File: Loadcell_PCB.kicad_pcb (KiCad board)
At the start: 2 copper layers, 57.5 x 74.5 mm, 52 parts, among them J1 USB_C_Receptacle_USB2.0, J2 Load cell side, J3 Micro_SD_Card, Q1 S8550, SW1 RESET, U1 ATmega328P-M, U4 HX711, U5 74125, U6 LD1117S33TR_SOT223, U7 CH340C, Y1 16MHz

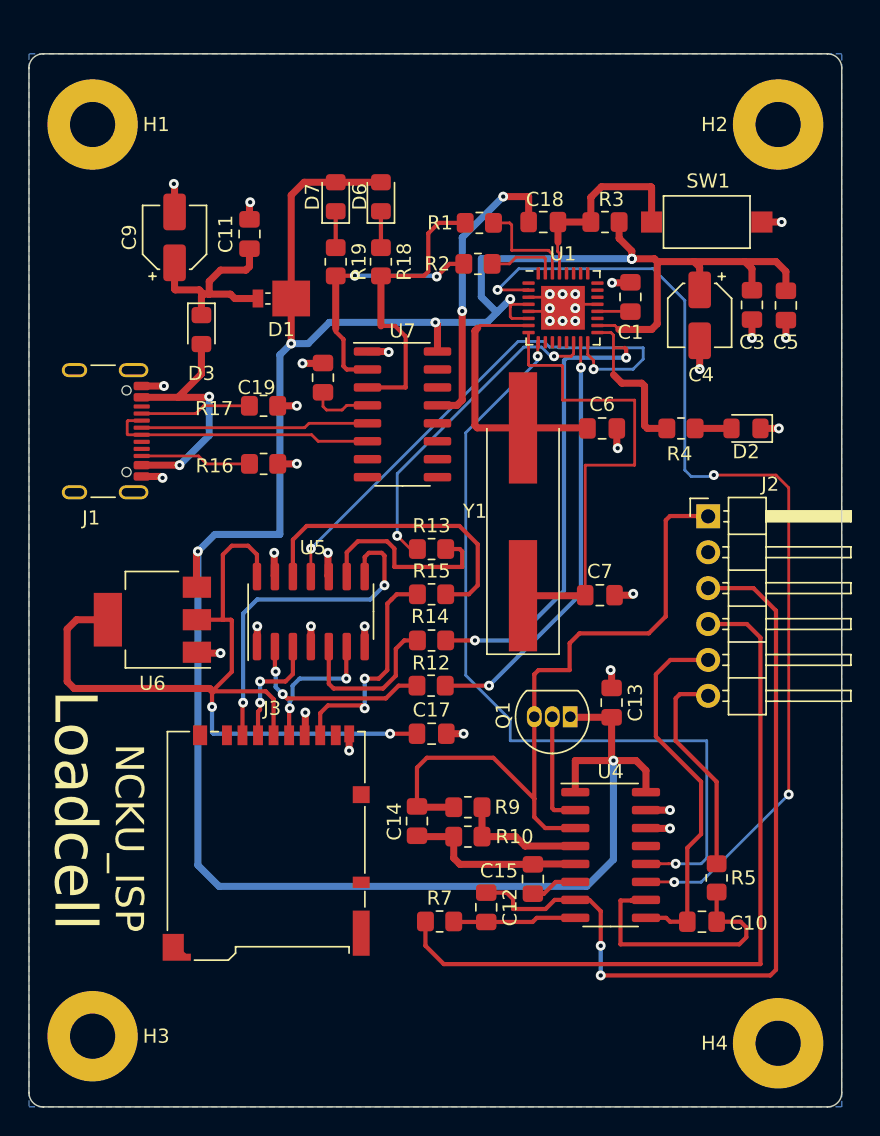
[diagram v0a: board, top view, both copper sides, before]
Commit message: some cleanup and add .gitignore
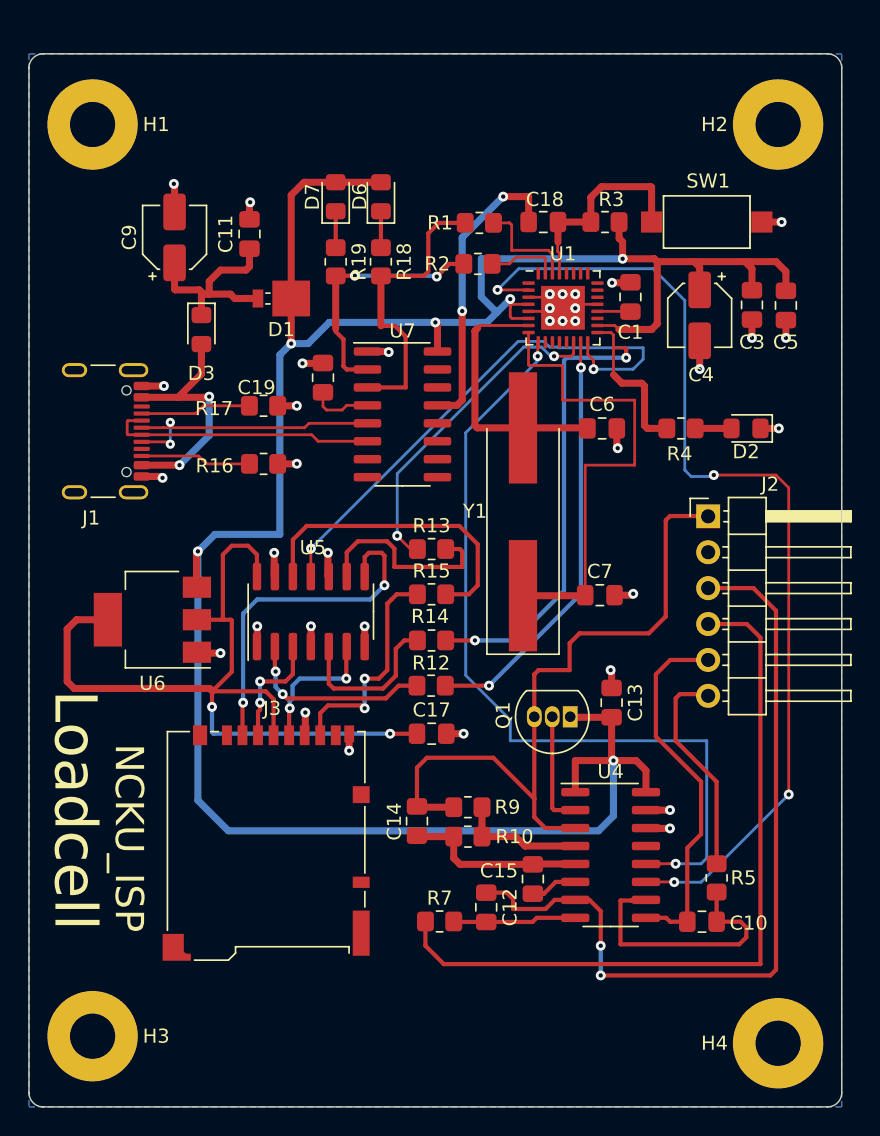
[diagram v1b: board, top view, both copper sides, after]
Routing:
- net +5V: track 181.8 -> 173.8 mm, vias 7 -> 6
- net /D+: track 16.1 -> 20.1 mm, vias 0 -> 2

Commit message: further cleanup for temp file
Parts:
- removed the C11 at (88.1, 35.1)
- removed the C4 at (120.0, 40.9)
- removed the C9 at (82.8, 35.4)
- removed the D1 at (90.4, 39.7)
- added C2: 4u7F_16V, Capacitor_SMD:CP_Elec_4x3, F.Cu at (80.9, 34.8)
- added C3: 100nF, Capacitor_SMD:C_0805_2012Metric_Pad1.18x1.45mm_HandSolder, F.Cu at (86.6, 34.7)
- C6: renamed from C5; value 1uF -> 100nF
- moved C6 2.45 mm to (123.6, 40.1)
- moved C4 2.45 mm to (126.1, 40.1)
- renumbered C12 to C11, C13 to C12, C14 to C13, C15 to C14, C17 to C15, C3 to C4, C19 to C5, C6 to C7, C7 to C8, C18 to C9, D3 to D1, D6 to D3, D7 to D4, R17 to R1, R7 to R10, R9 to R11, R10 to R12, R12 to R13, R13 to R14, R14 to R15, R15 to R16, R16 to R2, R1 to R3, R2 to R4, R3 to R5, R4 to R6, R18 to R7, R19 to R8, R5 to R9, U7 to U2, U4 to U3, U5 to U4, U6 to U5
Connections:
- D1 pad 1: VBUS -> +5V
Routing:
- net VBUS: track 15.0 -> 0.00 mm
- net +5V: track 173.8 -> 187.0 mm
- net GND: track 49.4 -> 47.6 mm, vias 36 -> 35
- net /VUSB: track 17.6 -> 18.4 mm
- net /SD_VCC: track 60.0 -> 59.4 mm
- net Net-(J2-Pin_1): track 50.6 -> 50.1 mm

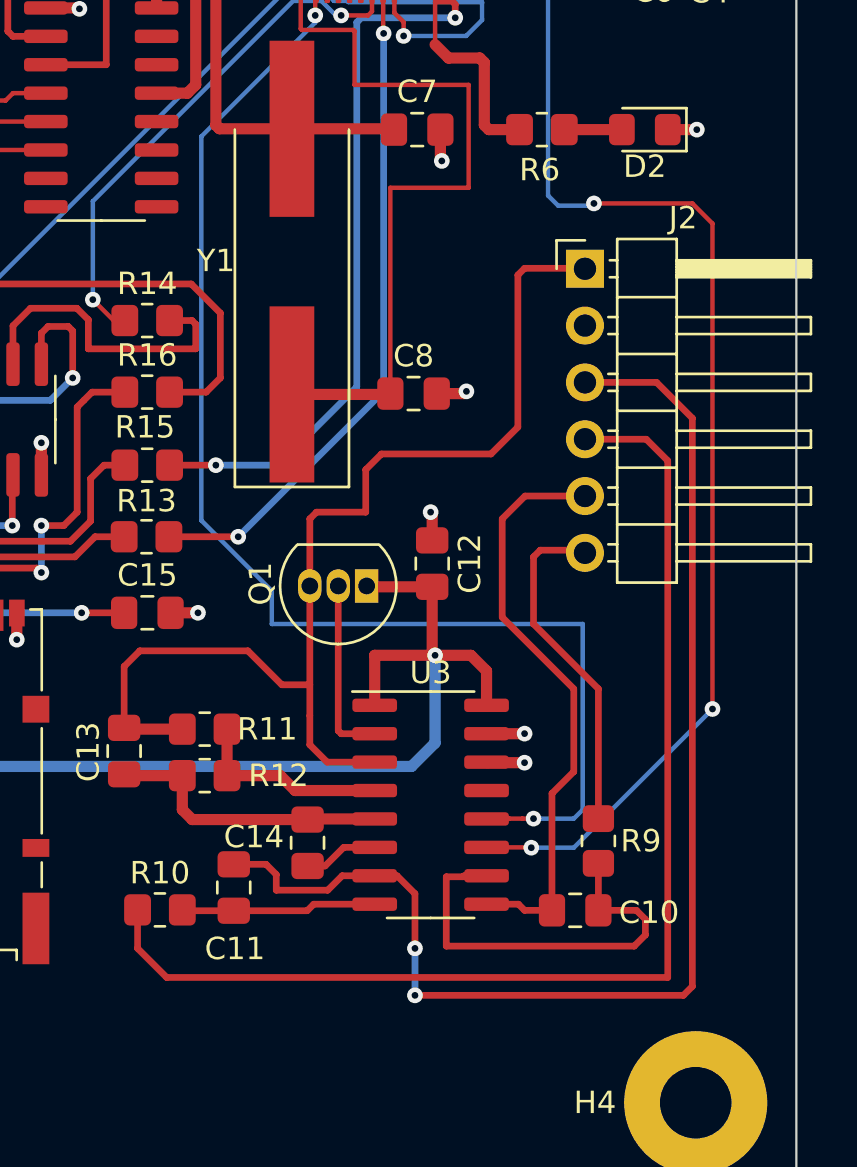
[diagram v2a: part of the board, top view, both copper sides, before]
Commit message: Add pull-up resistor at rate pin on HX711 IC
Since HX711 can work in a higher frequency with rate pin pulled up, so I
add a optional structure that can select between two frequency by
soldering a ball at solder-jump bridge
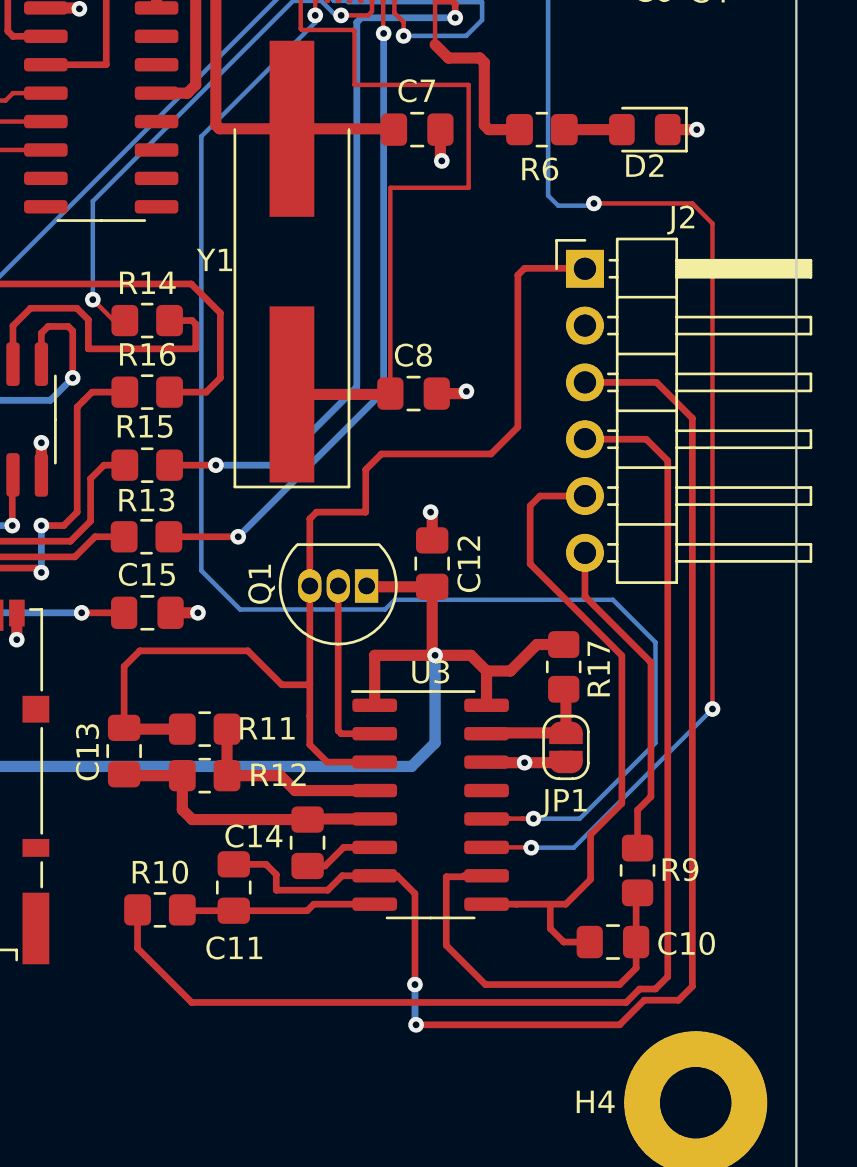
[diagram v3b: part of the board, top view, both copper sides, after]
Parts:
- added JP1: SolderJumper_2_Open, Jumper:SolderJumper-2_P1.3mm_Open_RoundedPad1.0x1.5mm, F.Cu at (119.7, 76.5)
- added R17: 1k, Resistor_SMD:R_0805_2012Metric_Pad1.20x1.40mm_HandSolder, F.Cu at (119.6, 72.9)
- moved C10 2.20 mm to (121.8, 85.2)
- moved R9 2.19 mm to (122.9, 82.0)
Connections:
- U3 pad 15: GND -> Net-(JP1-B)
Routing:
- net Net-(JP1-B): track 0.00 -> 5.56 mm
- net /DT: track 58.3 -> 63.4 mm
- net +5V: track 187.0 -> 190.9 mm
- net Net-(J2-Pin_5): track 26.4 -> 29.8 mm
- net Net-(J2-Pin_3): track 57.6 -> 59.4 mm
- net Net-(U3-INB+): track 19.1 -> 18.0 mm
- net Net-(J2-Pin_4): track 53.2 -> 54.1 mm
- net Net-(J2-Pin_6): track 15.4 -> 14.7 mm
- net GND: track 47.6 -> 47.8 mm, vias 35 -> 34

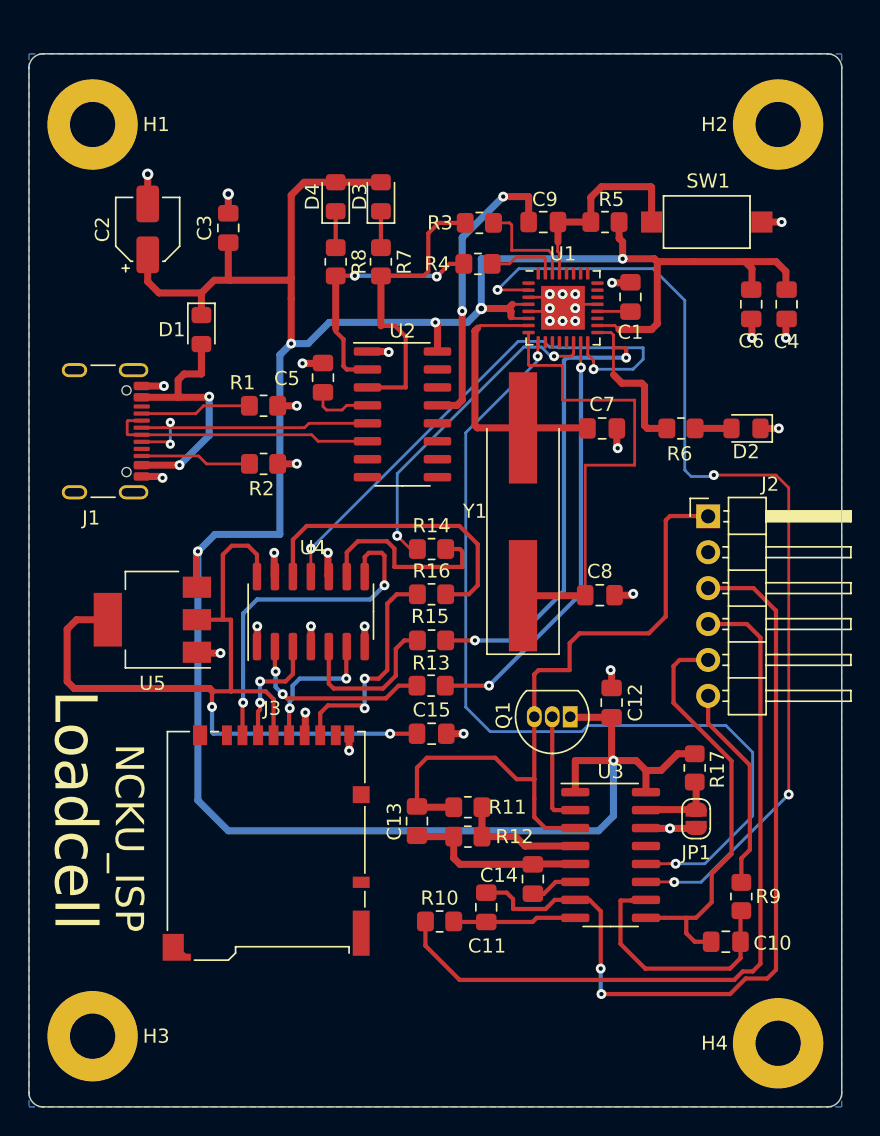
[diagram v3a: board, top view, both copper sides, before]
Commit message: Add an extra UART channel for GPS
In order to recieve GPS and serail print signals at the same time,
we need more than only one UART channel which is used as the serial
print channel by default, So now the second UART channel is added
and the implementation will be done by software.
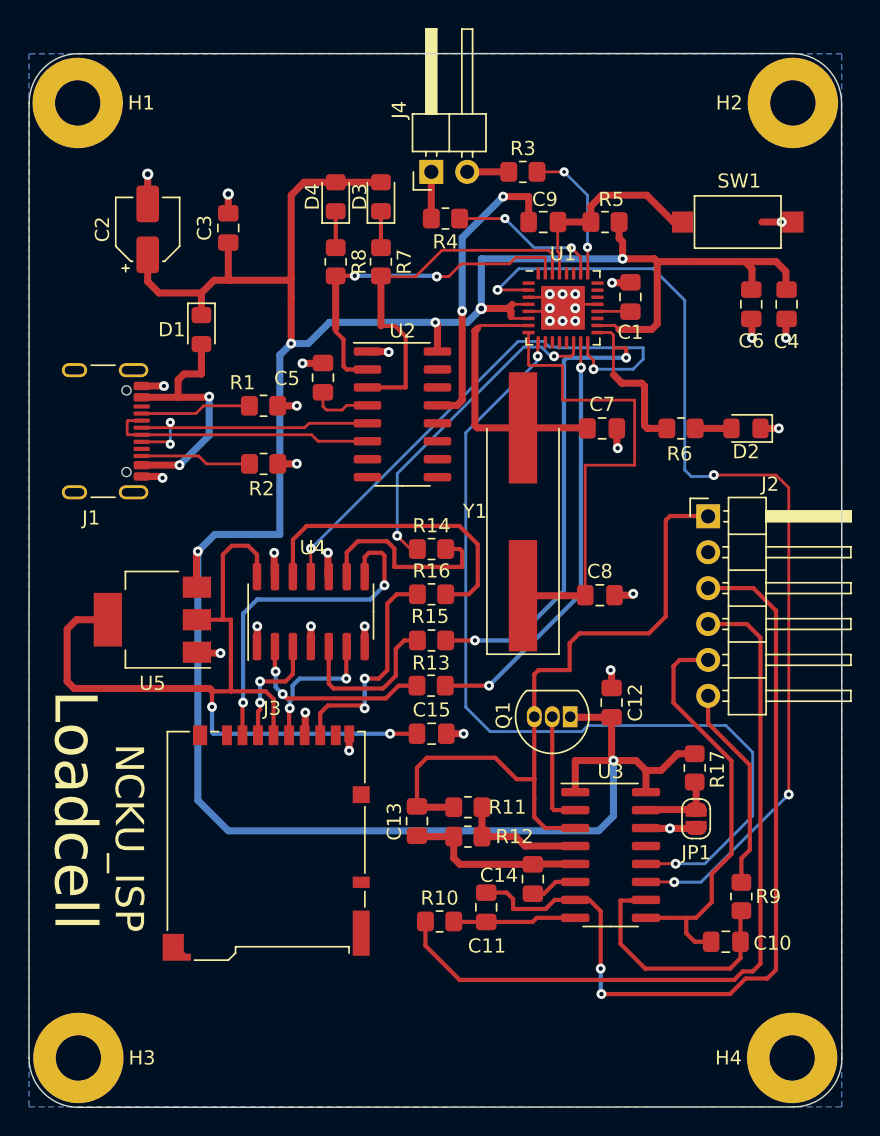
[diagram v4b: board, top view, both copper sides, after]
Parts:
- added J4: GPS, Connector_PinHeader_2.54mm:PinHeader_1x02_P2.54mm_Horizontal, F.Cu at (101.0, 30.7)
- JP1: value SolderJumper_2_Open -> pull up
- R3, R4: value 1K -> 330
- moved R3 4.74 mm to (107.4, 30.7)
- moved R4 3.94 mm to (102.0, 34.0)
- moved SW1 2.19 mm to (122.6, 34.3)
- moved H1 1.85 mm to (75.9, 25.9)
- moved H2 1.85 mm to (126.5, 25.9)
- moved H3 1.84 mm to (76.0, 93.4)
- moved H4 1.44 mm to (126.5, 93.4)
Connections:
- R3 pad 1: Net-(U1-PD0) -> Net-(U1-PC2)
- R3 pad 2: /TX -> /TX2
- R4 pad 1: Net-(U1-PD1) -> Net-(U1-PC3)
- R4 pad 2: /RX -> /RX2
- U1 pad 25: unconnected-(U1-PC2-Pad25) -> Net-(U1-PC2)
- U1 pad 26: unconnected-(U1-PC3-Pad26) -> Net-(U1-PC3)
- U1 pad 30: Net-(U1-PD0) -> /TX
- U1 pad 31: Net-(U1-PD1) -> /RX
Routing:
- net Net-(U1-PC3): track 0.00 -> 10.8 mm, vias 0 -> 2
- net Net-(U1-PC2): track 0.00 -> 9.79 mm, vias 0 -> 2
- net Net-(U1-PD0): track 7.49 -> 0.00 mm
- net /RX: track 17.9 -> 24.9 mm
- net /TX: track 21.0 -> 26.3 mm
- net Net-(U1-PD1): track 5.04 -> 0.00 mm
- net /RX2: track 0.00 -> 3.30 mm
- net /TX2: track 0.00 -> 2.94 mm
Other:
- board size 57.5 x 74.5 mm -> 57.5 x 74.6 mm
